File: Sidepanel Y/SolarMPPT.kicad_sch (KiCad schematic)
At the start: 46 parts, among them U11 INA180A4, U12 INA180A4

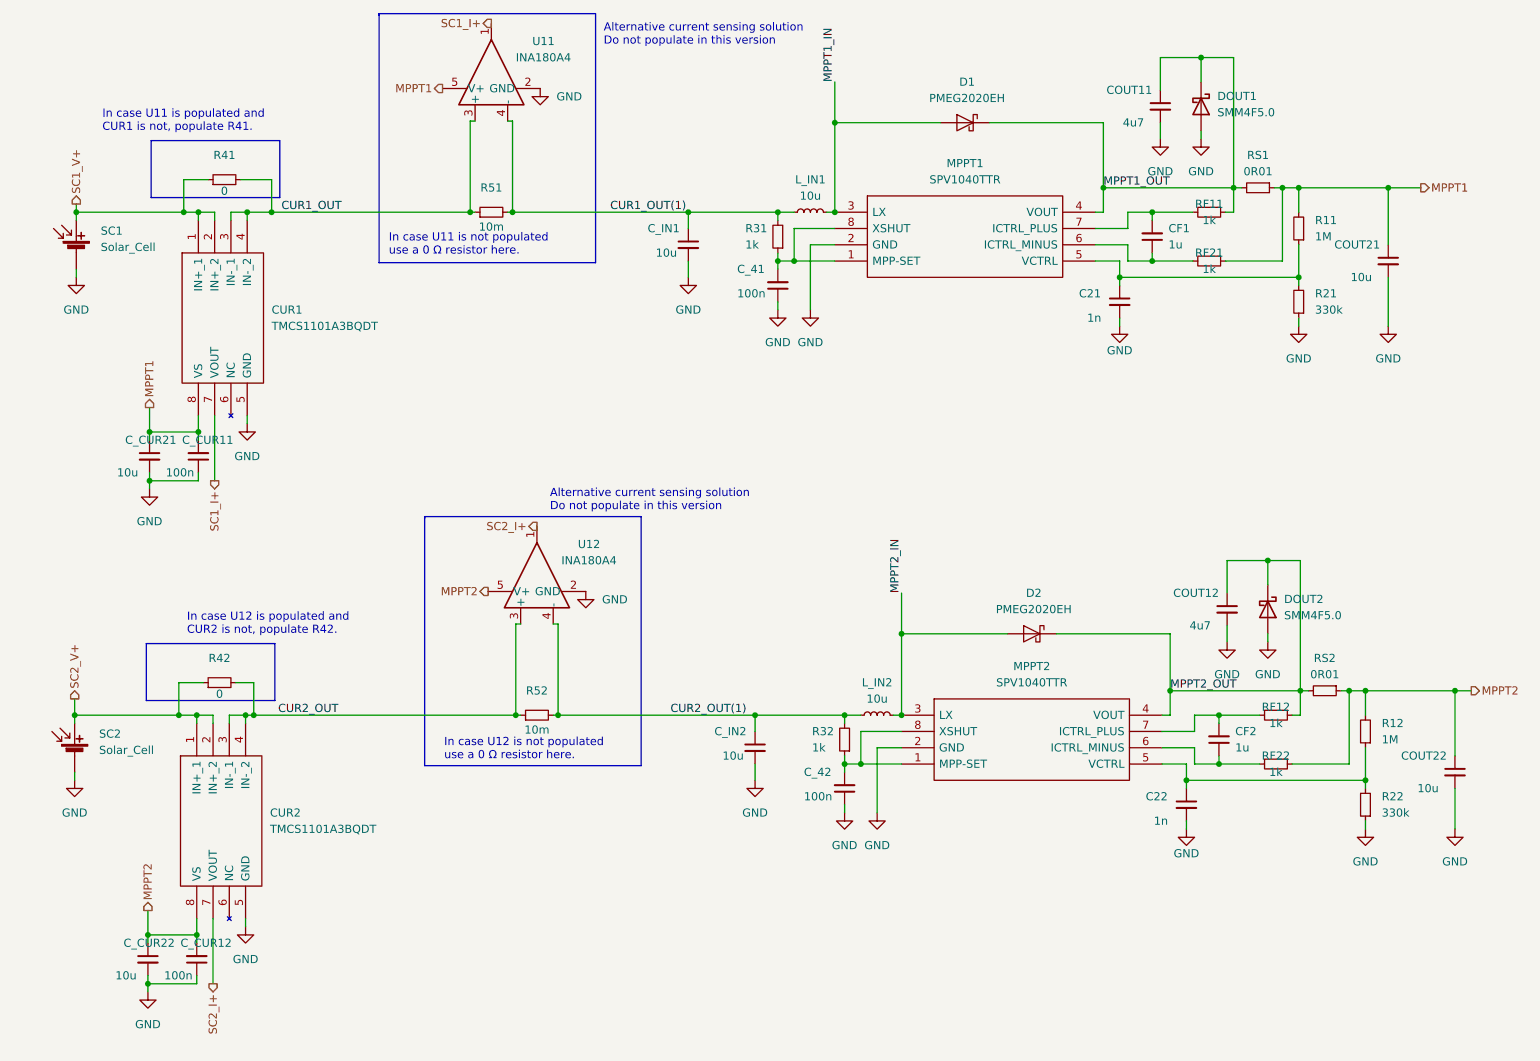
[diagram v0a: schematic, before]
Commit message: Changed the layout of all the sidepanel PCBs to mitigate the problems that arised from the bad previous design.
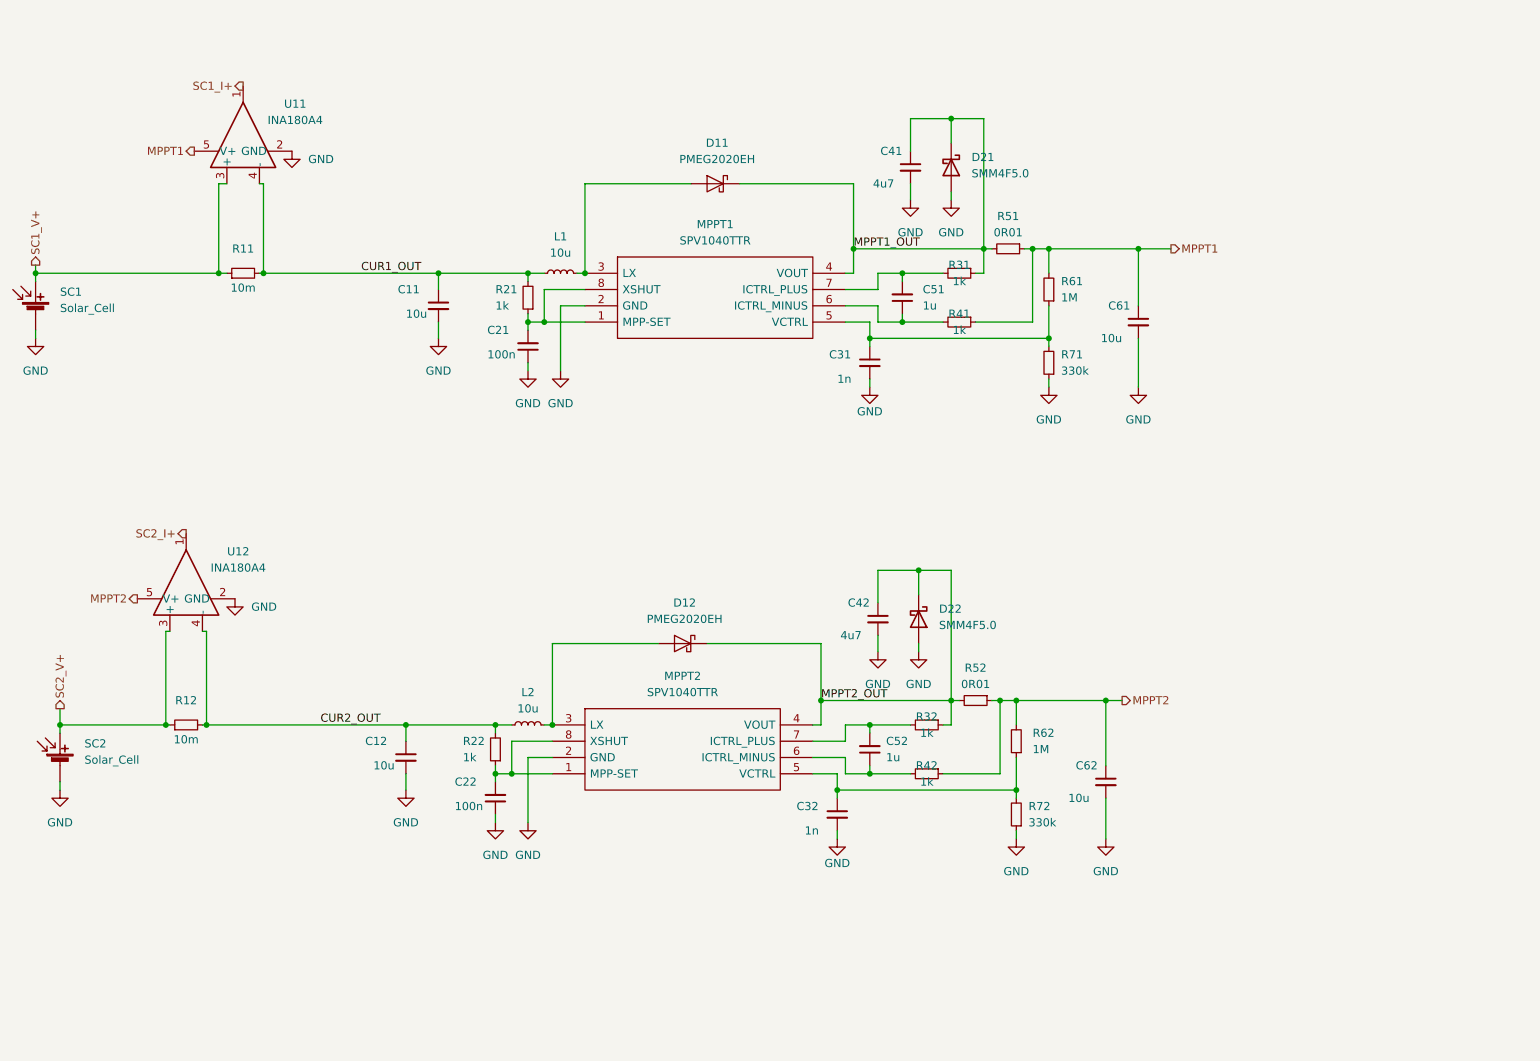
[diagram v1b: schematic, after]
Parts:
- removed CUR1, CUR2: TMCS1101A3BQDT, Package_SO:SOIC-8_3.9x4.9mm_P1.27mm, symbol SamacSys_Parts:TMCS1101A3BQDT
- removed C_CUR11, C_CUR12: 100n, Capacitor_SMD:C_0603_1608Metric, symbol Device:C_Small
- removed C_CUR21, C_CUR22: 10u, Capacitor_SMD:C_0603_1608Metric, symbol Device:C_Small
- removed R41, R42: 0, Resistor_SMD:R_0603_1608Metric, symbol Device:R_Small
- D21: renamed from DOUT1; footprint SamacSys:STMITE -> STS_semiconductor:DIO_SMM4F5.0A-TR
- D22: renamed from DOUT2; footprint SamacSys:STMITE -> STS_semiconductor:DIO_SMM4F5.0A-TR
- L1: renamed from L_IN1; footprint STS_Inductor_SMD:XAL6060103MEC -> STS_Inductor_SMD:IND_XAL6060-103MEC
- L2: renamed from L_IN2; footprint STS_Inductor_SMD:XAL6060103MEC -> STS_Inductor_SMD:IND_XAL6060-103MEC
- renumbered C_IN1 to C11, C_IN2 to C12, C_41 to C21, C_42 to C22, C21 to C31, C22 to C32, COUT11 to C41, COUT12 to C42, CF1 to C51, CF2 to C52, COUT21 to C61, COUT22 to C62, D1 to D11, D2 to D12, R51 to R11, R52 to R12, R31 to R21, R32 to R22, RF11 to R31, RF12 to R32, RF21 to R41, RF22 to R42, RS1 to R51, RS2 to R52, R11 to R61, R12 to R62, R21 to R71, R22 to R72
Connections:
- net CUR1_OUT(1) is gone; now on net CUR1_OUT: C11.1, L1.1, R11.2, R21.2, U11.4 (-)
- net CUR2_OUT(1) is gone; now on net CUR2_OUT: C12.1, L2.1, R12.2, R22.2, U12.4 (-)
- net CUR1_OUT: no longer R11.1, U11.3 (+)
- net CUR2_OUT: no longer R12.1, U12.3 (+)
- net SC1_V+: now also R11.1, U11.3 (+)
- net SC2_V+: now also R12.1, U12.3 (+)
- net MPPT1_IN: no longer names the net of D11.2 (A), L1.2, MPPT1.3 (LX)
- net MPPT2_IN: no longer names the net of D12.2 (A), L2.2, MPPT2.3 (LX)
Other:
- note removed: "Alternative current sensing solution Do not populate in this version"
- note removed: "In case U11 is not populated use a 0 Ω resistor here."
- note removed: "In case U11 is populated and CUR1 is not, populate R41."
- note removed: "In case U12 is not populated use a 0 Ω resistor here."
- note removed: "In case U12 is populated and CUR2 is not, populate R42."
- moved on the sheet: C11, C12, C21, C22, C31, C32, C41, C42, C51, C52, C61, C62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

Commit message: moved the connectors, changed the footprint of the input and output capacitors and splitted the input capacitor in two
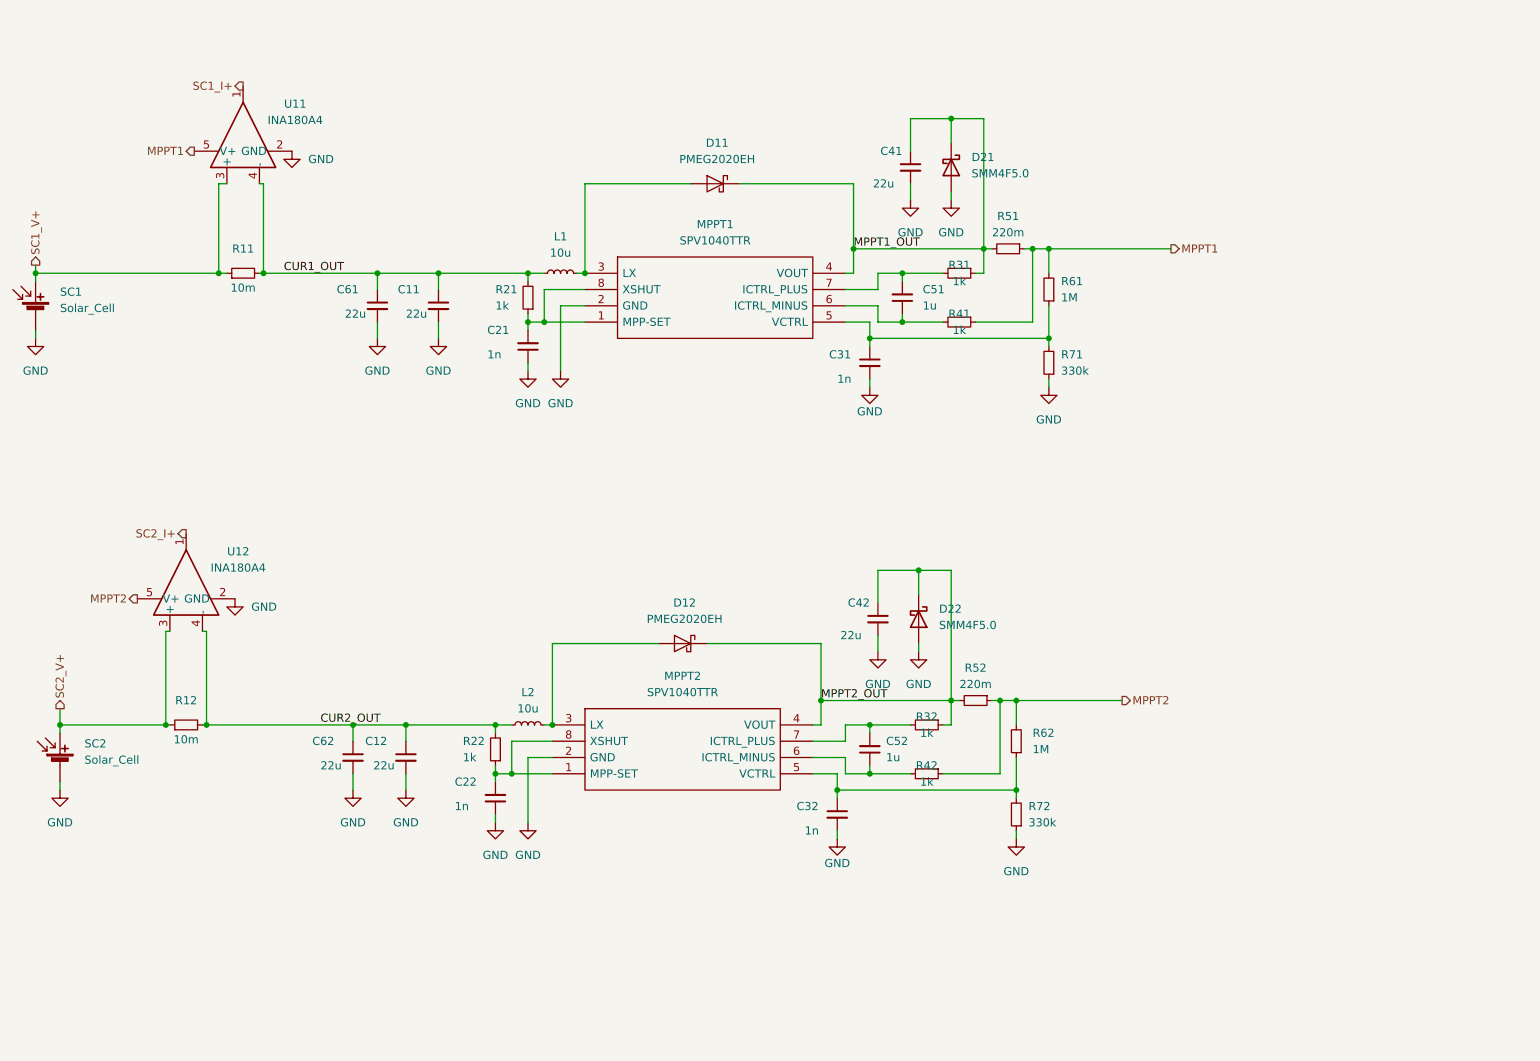
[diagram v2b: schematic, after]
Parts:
- C11, C12, C61, C62: value 10u -> 22u; footprint Capacitor_SMD:C_0603_1608Metric -> Capacitor_SMD:C_0805_2012Metric
- C21, C22: value 100n -> 1n
- C41, C42: value 4u7 -> 22u; footprint Capacitor_SMD:C_0603_1608Metric -> Capacitor_SMD:C_0805_2012Metric
- R11, R12: footprint Resistor_SMD:R_0603_1608Metric -> Resistor_SMD:R_0805_2012Metric
- R51, R52: value 0R01 -> 220m; footprint Resistor_SMD:R_0603_1608Metric -> Resistor_SMD:R_0805_2012Metric
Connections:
- net CUR1_OUT: now also C61.1
- net CUR2_OUT: now also C62.1
- net MPPT1: no longer C61.1
- net MPPT2: no longer C62.1

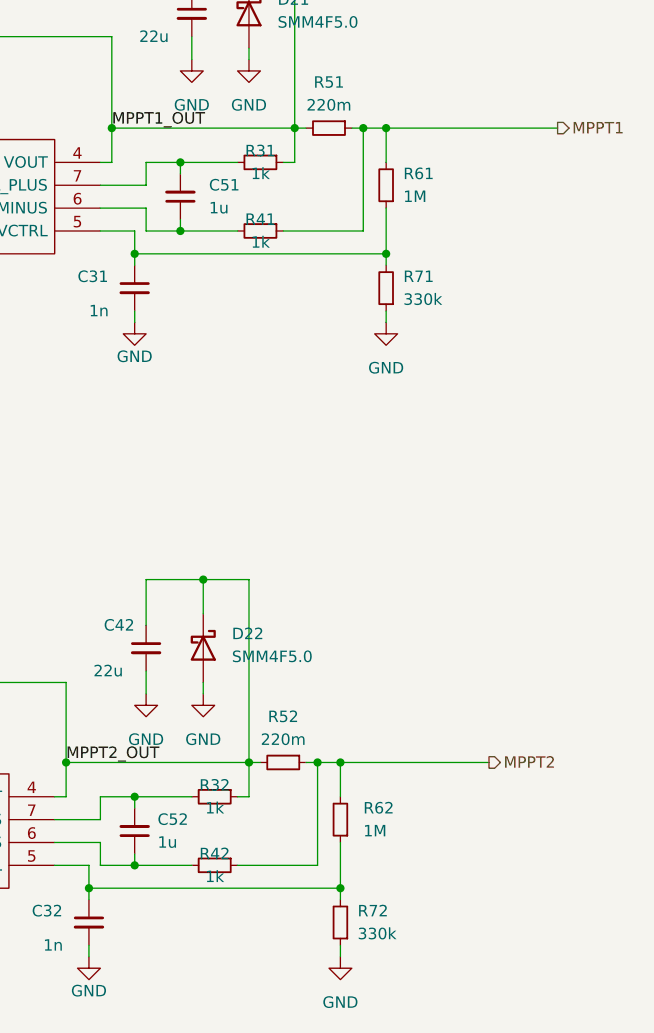
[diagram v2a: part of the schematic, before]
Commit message: Changed the values of the VCTRL resistors.
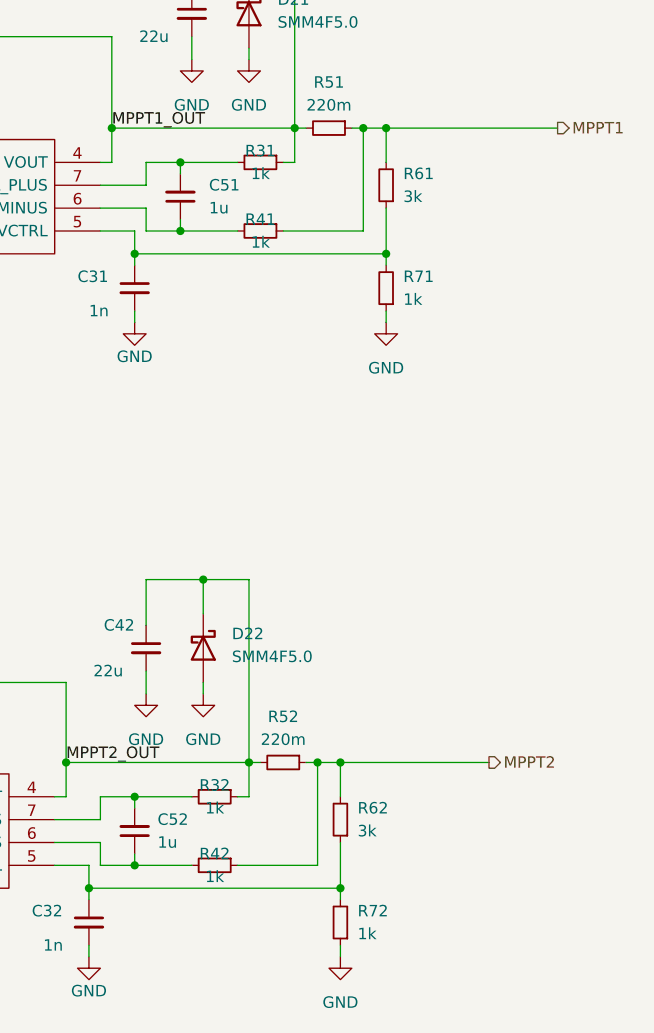
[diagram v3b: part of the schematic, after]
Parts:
- R61, R62: value 1M -> 3k
- R71, R72: value 330k -> 1k

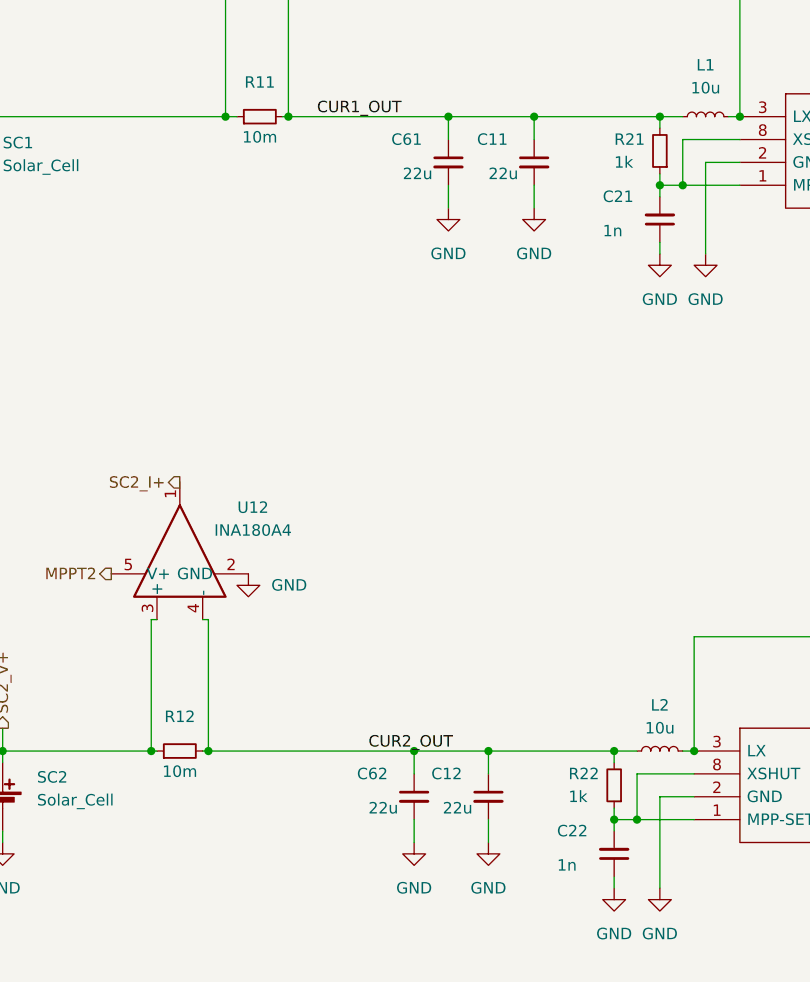
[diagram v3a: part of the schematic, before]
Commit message: Changed one of the inputs capacitors for all panels with one of 1 uF and lower ESR and moved some traces that were under the inductor.
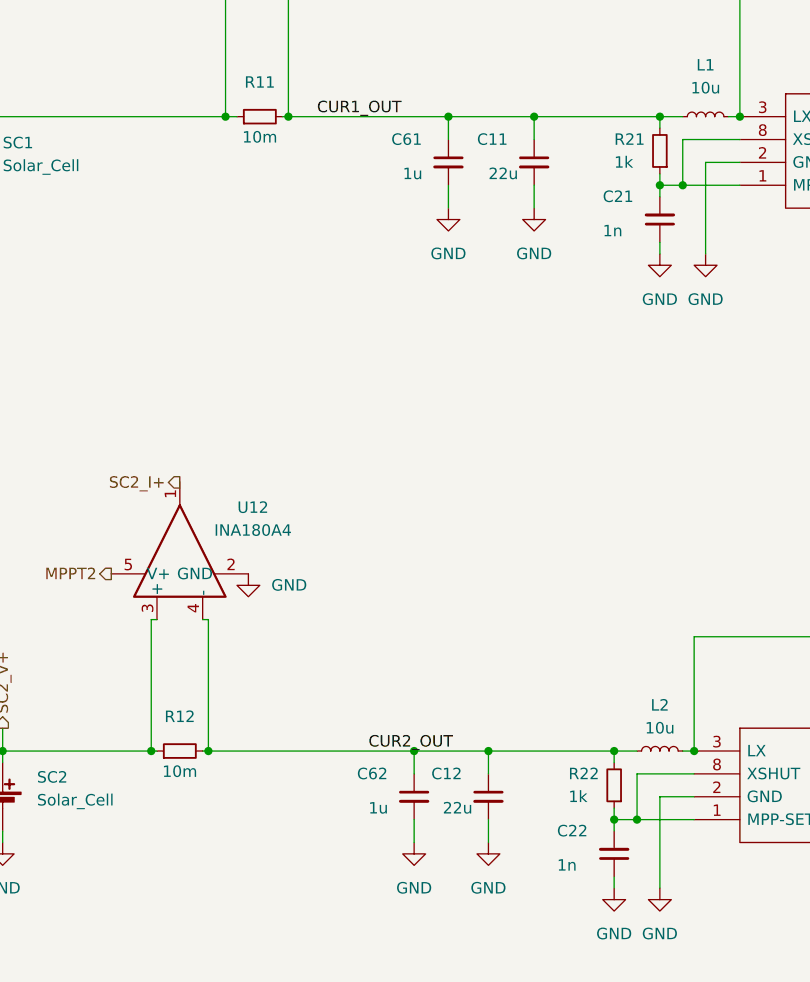
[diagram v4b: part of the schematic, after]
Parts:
- C61, C62: value 22u -> 1u
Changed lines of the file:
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@@
 			)
 		)
-		(property "Value" "22u"
+		(property "Value" "1u"
 			(at 77.47 133.35 0)
 			(effects
@@
 			)
 		)
-		(property "Description" ""
+		(property "Description" "TMK212B7105KGHTR"
 			(at 82.55 132.08 0)
 			(effects
@@
 			)
 		)
-		(property "Value" "22u"
+		(property "Value" "1u"
 			(at 81.28 62.865 0)
 			(effects
@@
 			)
 		)
-		(property "Description" ""
+		(property "Description" "TMK212B7105KGHTR"
 			(at 86.36 61.595 0)
 			(effects
